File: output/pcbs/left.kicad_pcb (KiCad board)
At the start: 2 copper layers, 279 x 108 mm, 71 parts

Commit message: TO-DO: aux bits on the PCB (battery, reset, and on/off)
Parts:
- removed S36, S37, S38, S39, S40, S41, S42, S43, S44, S45, S46, S47, S48, S49, S50, S51, S52, S53, S54, S55, S56, S57, S58, S59, S60, S61, S62, S63, S64, S65, S66, S67, S68, S69, S70: , MX
- added D1: , ComboDiode, F.Cu at (0.00, 5.00)
- added D10: , ComboDiode, F.Cu at (19.0, -71.0)
- added D11: , ComboDiode, F.Cu at (38.0, 2.00)
- added D12: , ComboDiode, F.Cu at (38.0, -17.0)
- added D13: , ComboDiode, F.Cu at (38.0, -36.0)
- added D14: , ComboDiode, F.Cu at (38.0, -55.0)
- added D15: , ComboDiode, F.Cu at (38.0, -74.0)
- added D16: , ComboDiode, F.Cu at (57.0, -20.0)
- added D17: , ComboDiode, F.Cu at (57.0, -39.0)
- added D18: , ComboDiode, F.Cu at (57.0, -58.0)
- added D19: , ComboDiode, F.Cu at (57.0, -77.0)
- added D2: , ComboDiode, F.Cu at (0.00, -14.0)
- added D20: , ComboDiode, F.Cu at (57.0, -96.0)
- added D21: , ComboDiode, F.Cu at (76.0, -25.0)
- added D22: , ComboDiode, F.Cu at (76.0, -44.0)
- added D23: , ComboDiode, F.Cu at (76.0, -63.0)
- added D24: , ComboDiode, F.Cu at (76.0, -82.0)
- added D25: , ComboDiode, F.Cu at (76.0, -101.0)
- added D26: , ComboDiode, F.Cu at (95.0, -20.0)
- added D27: , ComboDiode, F.Cu at (95.0, -39.0)
- added D28: , ComboDiode, F.Cu at (95.0, -58.0)
- added D29: , ComboDiode, F.Cu at (95.0, -77.0)
- added D3: , ComboDiode, F.Cu at (0.00, -33.0)
- added D30: , ComboDiode, F.Cu at (95.0, -96.0)
- added D31: , ComboDiode, F.Cu at (114.0, -14.0)
- added D32: , ComboDiode, F.Cu at (114.0, -33.0)
- added D33: , ComboDiode, F.Cu at (114.0, -52.0)
- added D34: , ComboDiode, F.Cu at (114.0, -71.0)
- added D35: , ComboDiode, F.Cu at (114.0, -90.0)
- added D4: , ComboDiode, F.Cu at (0.00, -52.0)
- added D5: , ComboDiode, F.Cu at (0.00, -71.0)
- added D6: , ComboDiode, F.Cu at (19.0, 5.00)
- added D7: , ComboDiode, F.Cu at (19.0, -14.0)
- added D8: , ComboDiode, F.Cu at (19.0, -33.0)
- added D9: , ComboDiode, F.Cu at (19.0, -52.0)
- moved MCU1 74.0 mm to (104.5, 0.00), turned to 180 degrees
- moved S16 19.0 mm to (57.0, -25.0)
- moved S17 19.0 mm to (57.0, -44.0)
- moved S18 19.0 mm to (57.0, -63.0)
- moved S19 19.0 mm to (57.0, -82.0)
- moved S20 19.0 mm to (57.0, -101.0)
- moved S21 19.0 mm to (76.0, -30.0)
- moved S22 19.0 mm to (76.0, -49.0)
- moved S23 19.0 mm to (76.0, -68.0)
- moved S24 19.0 mm to (76.0, -87.0)
- moved S25 19.0 mm to (76.0, -106.0)
- moved S26 19.0 mm to (95.0, -25.0)
- moved S27 19.0 mm to (95.0, -44.0)
- moved S28 19.0 mm to (95.0, -63.0)
- moved S29 19.0 mm to (95.0, -82.0)
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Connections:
- S1 pad 1: (no net) -> P104
- S10 pad 1: (no net) -> P011
- S11 pad 1: (no net) -> P100
- S12 pad 1: (no net) -> P100
- S13 pad 1: (no net) -> P100
- S14 pad 1: (no net) -> P100
- S15 pad 1: (no net) -> P100
- S16 pad 1: (no net) -> P024
- S17 pad 1: (no net) -> P024
- S18 pad 1: (no net) -> P024
- S19 pad 1: (no net) -> P024
- S2 pad 1: (no net) -> P104
- S20 pad 1: (no net) -> P024
- S21 pad 1: (no net) -> P022
- S22 pad 1: (no net) -> P022
- S23 pad 1: (no net) -> P022
- S24 pad 1: (no net) -> P022
- S25 pad 1: (no net) -> P022
- S26 pad 1: (no net) -> P020
- S27 pad 1: (no net) -> P020
- S28 pad 1: (no net) -> P020
- S29 pad 1: (no net) -> P020
- S3 pad 1: (no net) -> P104
- S30 pad 1: (no net) -> P020
- S31 pad 1: (no net) -> P017
- S32 pad 1: (no net) -> P017
- S33 pad 1: (no net) -> P017
- S34 pad 1: (no net) -> P017
- S35 pad 1: (no net) -> P017
- S4 pad 1: (no net) -> P104
- S5 pad 1: (no net) -> P104
- S6 pad 1: (no net) -> P011
- S7 pad 1: (no net) -> P011
- S8 pad 1: (no net) -> P011
- S9 pad 1: (no net) -> P011
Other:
- board size 279 x 108 mm -> 137 x 129 mm

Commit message: right board
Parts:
- removed MCU1: nice_nano, nice_nano
- added D36: , ComboDiode, F.Cu at (353.5, 223.9)
- added D37: , ComboDiode, F.Cu at (348.6, 205.5)
- added D38: , ComboDiode, F.Cu at (343.7, 187.2)
- added D39: , ComboDiode, F.Cu at (338.8, 168.8)
- added D40: , ComboDiode, F.Cu at (333.9, 150.5)
- added D41: , ComboDiode, F.Cu at (335.2, 228.8)
- added D42: , ComboDiode, F.Cu at (330.3, 210.5)
- added D43: , ComboDiode, F.Cu at (325.3, 192.1)
- added D44: , ComboDiode, F.Cu at (320.4, 173.8)
- added D45: , ComboDiode, F.Cu at (315.5, 155.4)
- added D46: , ComboDiode, F.Cu at (316.0, 230.8)
- added D47: , ComboDiode, F.Cu at (311.1, 212.5)
- added D48: , ComboDiode, F.Cu at (306.2, 194.1)
- added D49: , ComboDiode, F.Cu at (301.3, 175.8)
- added D50: , ComboDiode, F.Cu at (296.4, 157.4)
- added D51: , ComboDiode, F.Cu at (292.0, 214.5)
- added D52: , ComboDiode, F.Cu at (287.1, 196.1)
- added D53: , ComboDiode, F.Cu at (282.2, 177.8)
- added D54: , ComboDiode, F.Cu at (277.2, 159.4)
- added D55: , ComboDiode, F.Cu at (272.3, 141.1)
- added D56: , ComboDiode, F.Cu at (272.4, 214.6)
- added D57: , ComboDiode, F.Cu at (267.4, 196.2)
- added D58: , ComboDiode, F.Cu at (262.5, 177.9)
- added D59: , ComboDiode, F.Cu at (257.6, 159.5)
- added D60: , ComboDiode, F.Cu at (252.7, 141.2)
- added D61: , ComboDiode, F.Cu at (255.3, 224.3)
- added D62: , ComboDiode, F.Cu at (250.4, 206.0)
- added D63: , ComboDiode, F.Cu at (245.5, 187.6)
- added D64: , ComboDiode, F.Cu at (240.5, 169.3)
- added D65: , ComboDiode, F.Cu at (235.6, 150.9)
- added D66: , ComboDiode, F.Cu at (238.5, 235.0)
- added D67: , ComboDiode, F.Cu at (233.6, 216.7)
- added D68: , ComboDiode, F.Cu at (228.7, 198.3)
- added D69: , ComboDiode, F.Cu at (223.7, 180.0)
- added D70: , ComboDiode, F.Cu at (218.8, 161.6)
- added S36: , MX, F.Cu at (352.2, 219.1)
- added S37: , MX, F.Cu at (347.3, 200.7)
- added S38: , MX, F.Cu at (342.4, 182.4)
- added S39: , MX, F.Cu at (337.5, 164.0)
- added S40: , MX, F.Cu at (332.6, 145.7)
- added S41: , MX, F.Cu at (333.9, 224.0)
- added S42: , MX, F.Cu at (329.0, 205.6)
- added S43: , MX, F.Cu at (324.0, 187.3)
- added S44: , MX, F.Cu at (319.1, 168.9)
- added S45: , MX, F.Cu at (314.2, 150.6)
- added S46: , MX, F.Cu at (314.8, 226.0)
- added S47: , MX, F.Cu at (309.8, 207.7)
- added S48: , MX, F.Cu at (304.9, 189.3)
- added S49: , MX, F.Cu at (300.0, 170.9)
- added S50: , MX, F.Cu at (295.1, 152.6)
- added S51: , MX, F.Cu at (290.7, 209.7)
- added S52: , MX, F.Cu at (285.8, 191.3)
- added S53: , MX, F.Cu at (280.9, 173.0)
- added S54: , MX, F.Cu at (276.0, 154.6)
- added S55: , MX, F.Cu at (271.0, 136.3)
- added S56: , MX, F.Cu at (271.1, 209.8)
- added S57: , MX, F.Cu at (266.1, 191.4)
- added S58: , MX, F.Cu at (261.2, 173.1)
- added S59: , MX, F.Cu at (256.3, 154.7)
- added S60: , MX, F.Cu at (251.4, 136.3)
- added S61: , MX, F.Cu at (254.0, 219.5)
- added S62: , MX, F.Cu at (249.1, 201.2)
- added S63: , MX, F.Cu at (244.2, 182.8)
- added S64: , MX, F.Cu at (239.2, 164.4)
- added S65: , MX, F.Cu at (234.3, 146.1)
- added S66: , MX, F.Cu at (237.2, 230.2)
- added S67: , MX, F.Cu at (232.3, 211.9)
- added S68: , MX, F.Cu at (227.4, 193.5)
- added S69: , MX, F.Cu at (222.4, 175.2)
- added S70: , MX, F.Cu at (217.5, 156.8)
- moved S35 260.2 mm to (179.5, 156.8), turned to -15 degrees
- moved D35 259.7 mm to (178.2, 161.6), turned to -15 degrees
- moved S34 258.4 mm to (174.6, 175.2), turned to -15 degrees
- moved D34 257.9 mm to (173.3, 180.0), turned to -15 degrees
- moved S33 256.6 mm to (169.7, 193.5), turned to -15 degrees
- moved S30 256.2 mm to (162.7, 146.1), turned to -15 degrees
- moved D33 256.2 mm to (168.4, 198.3), turned to -15 degrees
- moved D30 255.7 mm to (161.4, 150.9), turned to -15 degrees
- moved S32 255.0 mm to (164.8, 211.9), turned to -15 degrees
- moved D32 254.6 mm to (163.5, 216.7), turned to -15 degrees
- moved S29 254.3 mm to (157.8, 164.4), turned to -15 degrees
- moved D29 253.8 mm to (156.5, 169.3), turned to -15 degrees
- moved S31 253.4 mm to (159.9, 230.2), turned to -15 degrees
- moved D31 253.0 mm to (158.6, 235.0), turned to -15 degrees
- moved S28 252.5 mm to (152.9, 182.8), turned to -15 degrees
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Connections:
- D1 pad 1: P113 -> P031
- D10 pad 1: P031 -> P113
- D11 pad 1: P113 -> P031
- D12 pad 1: P115 -> P029
- D14 pad 1: P029 -> P115
- D15 pad 1: P031 -> P113
- D16 pad 1: P113 -> P031
- D17 pad 1: P115 -> P029
- D19 pad 1: P029 -> P115
- D2 pad 1: P115 -> P029
- D20 pad 1: P031 -> P113
- D21 pad 1: P113 -> P031
- D22 pad 1: P115 -> P029
- D24 pad 1: P029 -> P115
- D25 pad 1: P031 -> P113
- D26 pad 1: P113 -> P031
- D27 pad 1: P115 -> P029
- D29 pad 1: P029 -> P115
- D30 pad 1: P031 -> P113
- D31 pad 1: P113 -> P031
- D32 pad 1: P115 -> P029
- D34 pad 1: P029 -> P115
- D35 pad 1: P031 -> P113
- D4 pad 1: P029 -> P115
- D5 pad 1: P031 -> P113
- D6 pad 1: P113 -> P031
- D7 pad 1: P115 -> P029
- D9 pad 1: P029 -> P115
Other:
- board size 137 x 129 mm -> 162.1 x 139.6 mm

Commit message: basically done pcbs
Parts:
- removed D36, D37, D38, D39, D40, D41, D42, D43, D44, D45, D46, D47, D48, D49, D50, D51, D52, D53, D54, D55, D56, D57, D58, D59, D60, D61, D62, D63, D64, D65, D66, D67, D68, D69, D70: , ComboDiode
- removed S36, S37, S38, S39, S40, S41, S42, S43, S44, S45, S46, S47, S48, S49, S50, S51, S52, S53, S54, S55, S56, S57, S58, S59, S60, S61, S62, S63, S64, S65, S66, S67, S68, S69, S70: , MX
- added ?: , HOLE_M2_TH, F.Cu at (109.5, 190.5)
- added ?: , HOLE_M2_TH, F.Cu at (109.5, 133.5)
- added ?: , HOLE_M2_TH, F.Cu at (166.5, 141.5)
- added ?: , HOLE_M2_TH, F.Cu at (185.5, 108.5)
- added ?: , HOLE_M2_TH, F.Cu at (204.5, 184.5)
- added B1: Panasonic_EVQPUL_EVQPUC, Panasonic_EVQPUL_EVQPUC, F.Cu at (223.0, 184.0)
- added JST1: , JST_PH_S2B-PH-K_02x2.00mm_Angled, F.Cu at (214.0, 171.5)
- added MCU1: nice_nano, nice_nano, F.Cu at (204.5, 200.0)
- added T1: , E73:SPDT_C128955, F.Cu at (222.8, 168.0)
- moved D31 74.0 mm to (214.0, 186.0), turned to 0 degrees
- moved S31 73.2 mm to (214.0, 181.0), turned to 0 degrees
- moved D32 70.9 mm to (214.0, 167.0), turned to 0 degrees
- moved S32 70.1 mm to (214.0, 162.0), turned to 0 degrees
- moved D26 69.3 mm to (195.0, 180.0), turned to 0 degrees
- moved S26 68.4 mm to (195.0, 175.0), turned to 0 degrees
- moved D33 67.9 mm to (214.0, 148.0), turned to 0 degrees
- moved S33 67.2 mm to (214.0, 143.0), turned to 0 degrees
- moved D27 66.0 mm to (195.0, 161.0), turned to 0 degrees
- moved D34 65.2 mm to (214.0, 129.0), turned to 0 degrees
- moved S27 65.2 mm to (195.0, 156.0), turned to 0 degrees
- moved D21 64.8 mm to (176.0, 175.0), turned to 0 degrees
- moved S34 64.6 mm to (214.0, 124.0), turned to 0 degrees
- moved S21 63.9 mm to (176.0, 170.0), turned to 0 degrees
- moved D11 63.9 mm to (138.0, 202.0), turned to 0 degrees
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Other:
- board size 162.1 x 139.6 mm -> 137 x 129 mm
- board text added: "Icarus"

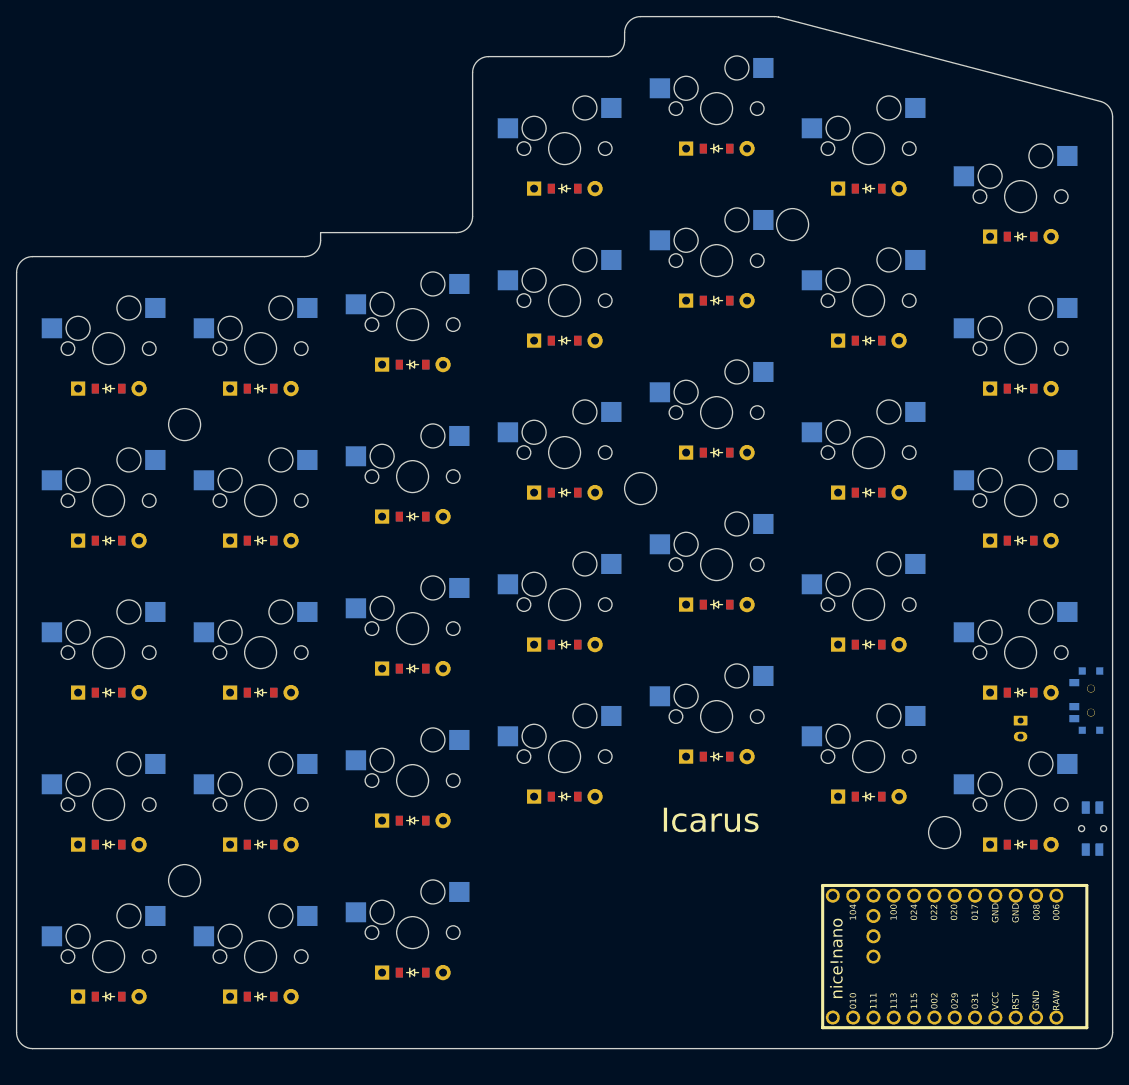
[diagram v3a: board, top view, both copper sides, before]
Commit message: redesign for short board, left but no right pcb. Final pcbs for old design
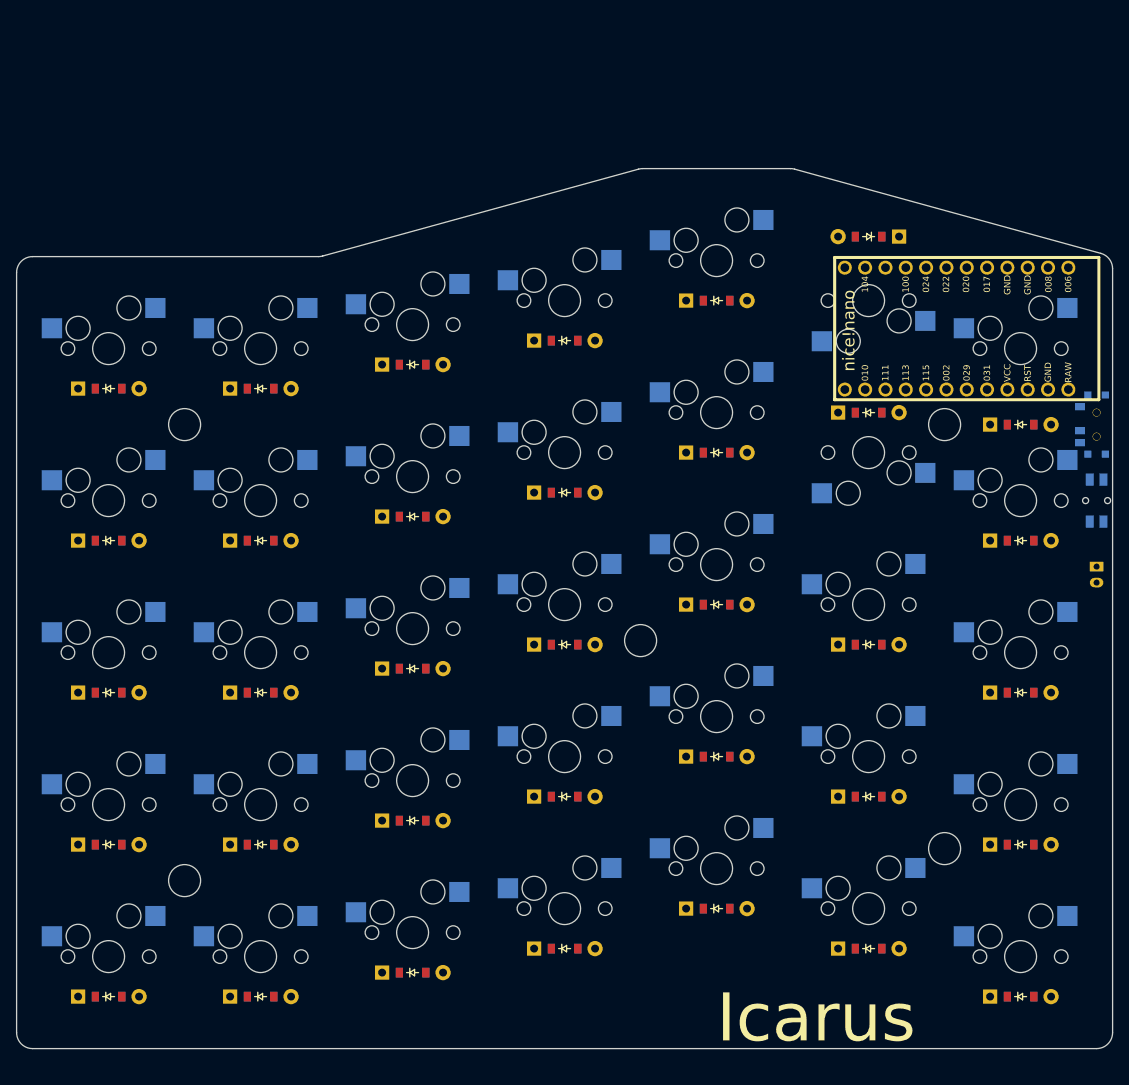
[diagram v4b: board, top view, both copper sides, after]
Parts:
- removed the ? at (166.5, 141.5)
- removed the ? at (185.5, 108.5)
- removed the ? at (204.5, 184.5)
- added ?: , HOLE_M2_TH, F.Cu at (166.5, 160.5)
- added ?: , HOLE_M2_TH, F.Cu at (204.5, 133.5)
- added ?: , HOLE_M2_TH, F.Cu at (204.5, 186.5)
- moved D29 84.2 mm to (214.0, 205.0)
- moved D30 84.2 mm to (214.0, 186.0)
- moved S29 84.2 mm to (214.0, 200.0)
- moved S30 84.2 mm to (214.0, 181.0)
- moved MCU1 78.5 mm to (206.0, 121.5)
- moved B1 41.0 mm to (223.5, 143.0)
- moved T1 34.5 mm to (223.5, 133.5)
- moved D34 26.9 mm to (195.0, 110.0), turned to 180 degrees
- moved D33 24.8 mm to (195.0, 132.0)
- moved D35 23.5 mm to (214.0, 133.5)
- moved S34 23.0 mm to (195.0, 137.0), turned to -180 degrees
- moved S35 23.0 mm to (195.0, 118.0), turned to -180 degrees
- moved JST1 21.5 mm to (223.5, 152.2)
- moved D16 19.0 mm to (157.0, 199.0)
- moved D17 19.0 mm to (157.0, 180.0)
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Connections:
- D1 pad 1: P031 -> P029
- D10 pad 1: P113 -> P031
- D11 pad 1: P031 -> P029
- D12 pad 1: P029 -> P002
- D13 pad 1: P002 -> P115
- D14 pad 1: P115 -> P113
- D15 pad 1: P113 -> P031
- D16 pad 1: P031 -> P029
- D17 pad 1: P029 -> P002
- D18 pad 1: P002 -> P115
- D19 pad 1: P115 -> P113
- D2 pad 1: P029 -> P002
- D20 pad 1: P113 -> P031
- D21 pad 1: P031 -> P029
- D22 pad 1: P029 -> P002
- D23 pad 1: P002 -> P115
- D24 pad 1: P115 -> P113
- D25 pad 1: P113 -> P031
- D26 pad 1: P031 -> P029
- D27 pad 1: P029 -> P002
- D28 pad 1: P002 -> P115
- D29 pad 1: P115 -> P029
- D29 pad 2: index_top -> inner_space
- D3 pad 1: P002 -> P115
- D30 pad 1: P113 -> P002
- D30 pad 2: index_num -> inner_bottom
- D31 pad 1: P031 -> P115
- D31 pad 2: inner_space -> inner_home
- D32 pad 1: P029 -> P113
- D32 pad 2: inner_bottom -> inner_top
- D33 pad 1: P002 -> P113
- D33 pad 2: inner_home -> index_top
- D34 pad 1: P115 -> P031
- D34 pad 2: inner_top -> index_num
- D35 pad 1: P113 -> P031
- D4 pad 1: P115 -> P113
- D5 pad 1: P113 -> P031
- D6 pad 1: P031 -> P029
- D7 pad 1: P029 -> P002
- D8 pad 1: P002 -> P115
- D9 pad 1: P115 -> P113
- S1 pad 1: P104 -> P024
- S10 pad 1: P011 -> P100
- S11 pad 1: P100 -> P011
- S12 pad 1: P100 -> P011
- S13 pad 1: P100 -> P011
- S14 pad 1: P100 -> P011
- S15 pad 1: P100 -> P011
- S16 pad 1: P024 -> P104
- S17 pad 1: P024 -> P104
- S18 pad 1: P024 -> P104
- S19 pad 1: P024 -> P104
- S2 pad 1: P104 -> P024
- S20 pad 1: P024 -> P104
- S21 pad 1: P022 -> P106
- S22 pad 1: P022 -> P106
- S23 pad 1: P022 -> P106
- S24 pad 1: P022 -> P106
- S25 pad 1: P022 -> P106
- S29 pad 1: P020 -> P017
- S29 pad 2: index_top -> inner_space
- S3 pad 1: P104 -> P024
- S30 pad 1: P020 -> P017
- S30 pad 2: index_num -> inner_bottom
- S31 pad 2: inner_space -> inner_home
- S32 pad 2: inner_bottom -> inner_top
- S33 pad 2: inner_home -> inner_num
- S34 pad 1: P017 -> P020
- S34 pad 2: inner_top -> index_top
- S35 pad 1: P017 -> P020
- S35 pad 2: inner_num -> index_num
- S4 pad 1: P104 -> P024
- S5 pad 1: P104 -> P024
- S6 pad 1: P011 -> P100
- S7 pad 1: P011 -> P100
- S8 pad 1: P011 -> P100
- S9 pad 1: P011 -> P100
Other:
- board size 137 x 129 mm -> 137 x 110 mm
